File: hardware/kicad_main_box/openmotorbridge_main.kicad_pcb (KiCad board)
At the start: 4 copper layers, 85 x 55 mm, 40 parts, among them J1 IDC_2X13_HEADER, J2 MicroSD_4Bit_SDIO, J3 USB_C_IP67, J4 LED_EXT, J5 BAT_LIPO_3V7, J6 NTC_10K_JEITA, T1 Bourns_LM-NP-1001_Audio1, T2 Bourns_LM-NP-1001_Audio2, U1 LM5164-Q1, U2 ESP32-S3-WROOM-1, U3 ES8388, U4 B0505S-1WR3, U5 BMI270, U6 TCAN334G, U7 TLP222A_Opto1, U8 TLP222A_Opto2, U9 TPS7A0533_LDO

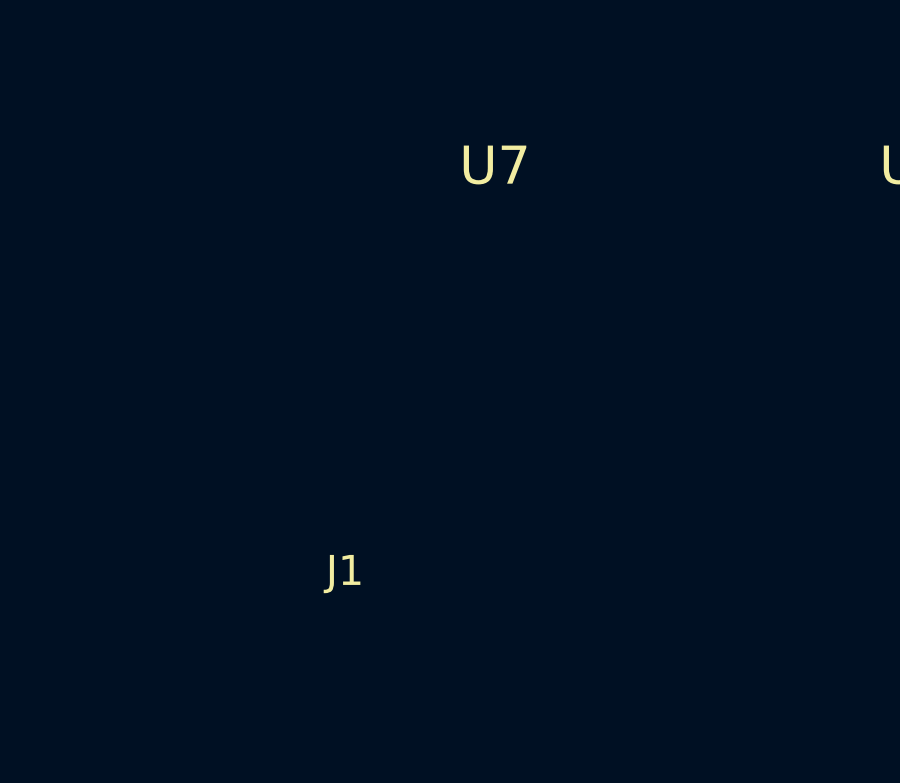
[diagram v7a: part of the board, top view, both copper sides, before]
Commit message: fix(pcb): finalize horizontal J1 layout on bottom edge with optimal straight audio routing
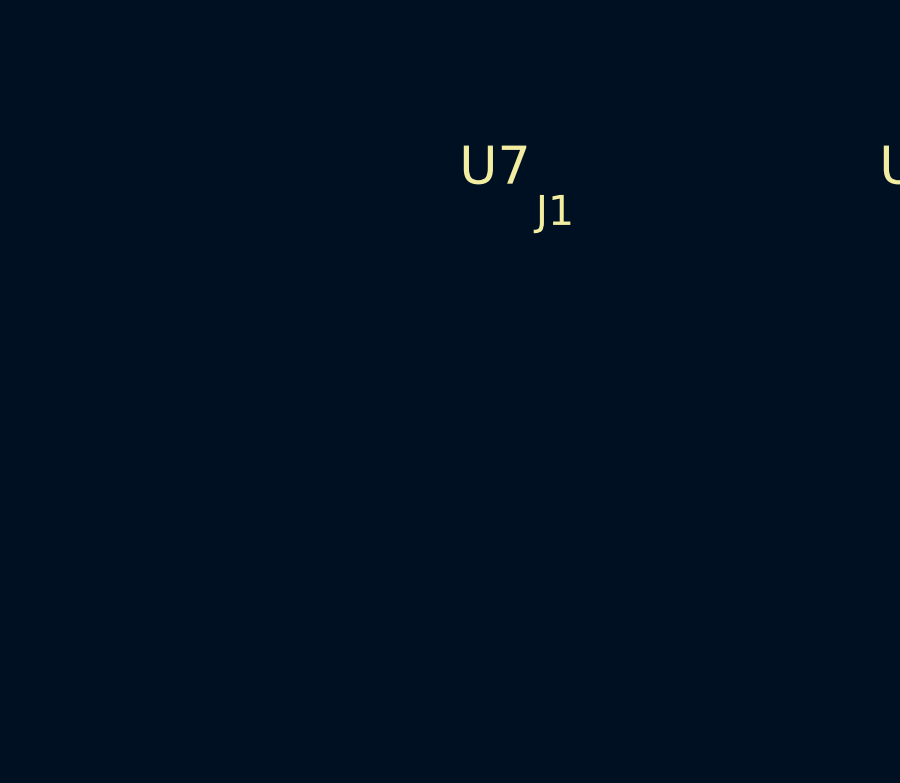
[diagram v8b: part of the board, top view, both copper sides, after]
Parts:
- moved J1 5.00 mm to (168.0, 118.5), turned to 0 degrees
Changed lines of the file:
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@@
 	(footprint "Connector_Dsub:DSUB-26-HD_Female_Horizontal_P2.29x1.98mm_EdgePinOffset7.70mm_Housings_POS01"
 		(layer "F.Cu")
-		(at 173.00 118.50 90.0)
+		(at 168.00 118.50)
 		(property "Reference" "J1"
 			(at 0 -12 180)
